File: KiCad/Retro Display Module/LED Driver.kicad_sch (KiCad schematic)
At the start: 30 parts, among them J23 Conn_01x02_Pin, J32 Conn_02x11_Odd_Even, U10 D882_C9634, U11 OP07CDR, U12 D882_C9634, U13 D882_C9634, U14 D882_C9634, U15 D882_C9634, U16 D882_C9634, U17 D882_C9634, U18 D882_C9634, U7 D882_C9634, U8 D882_C9634, U9 D882_C9634

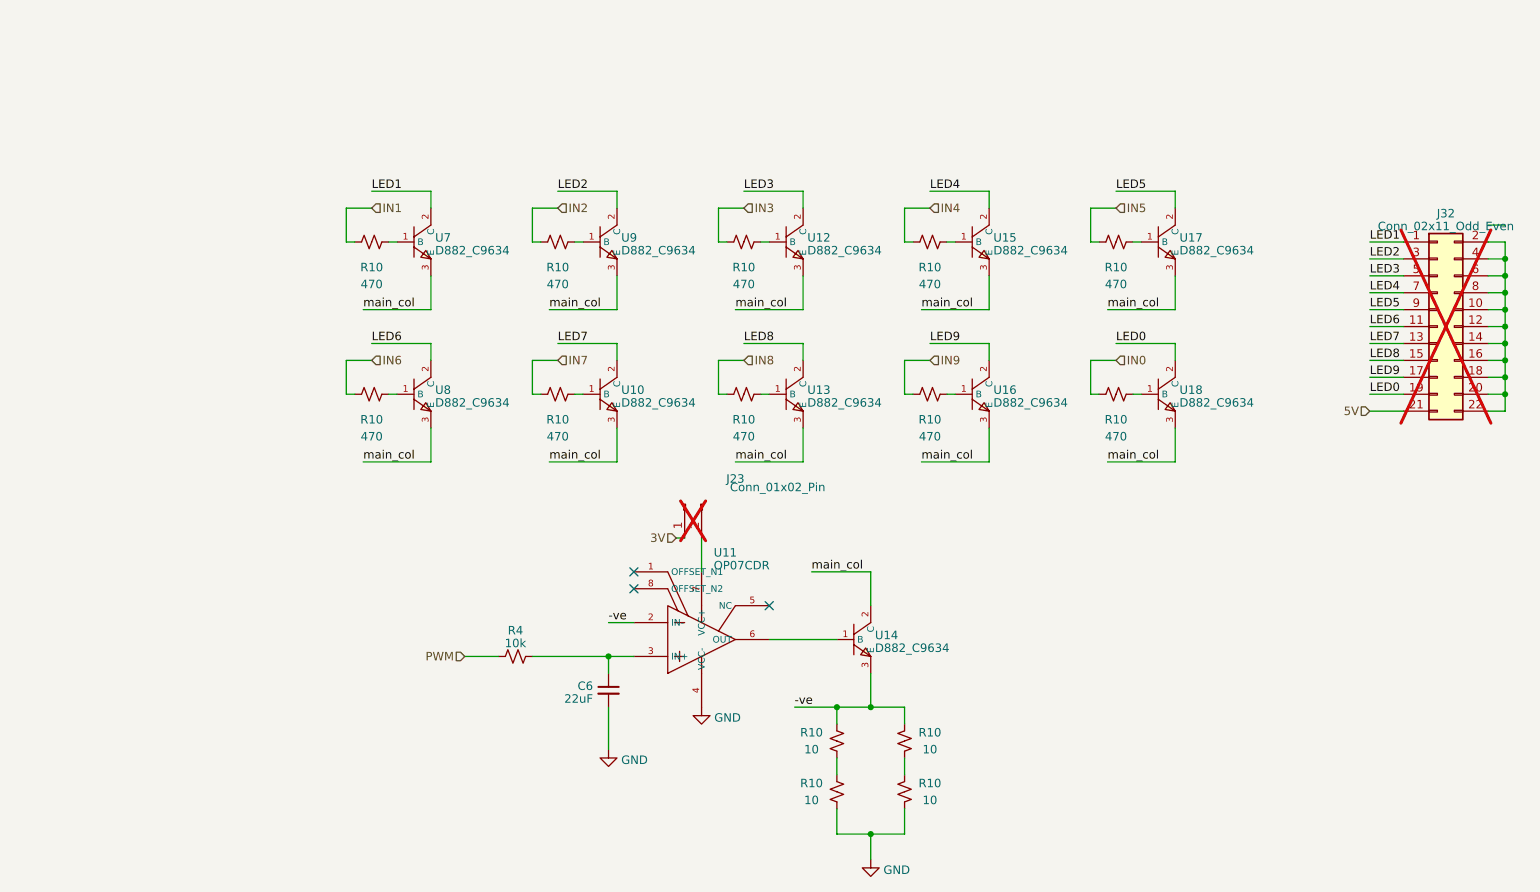
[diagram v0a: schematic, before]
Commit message: Updated USB PD and Driver LED circuit
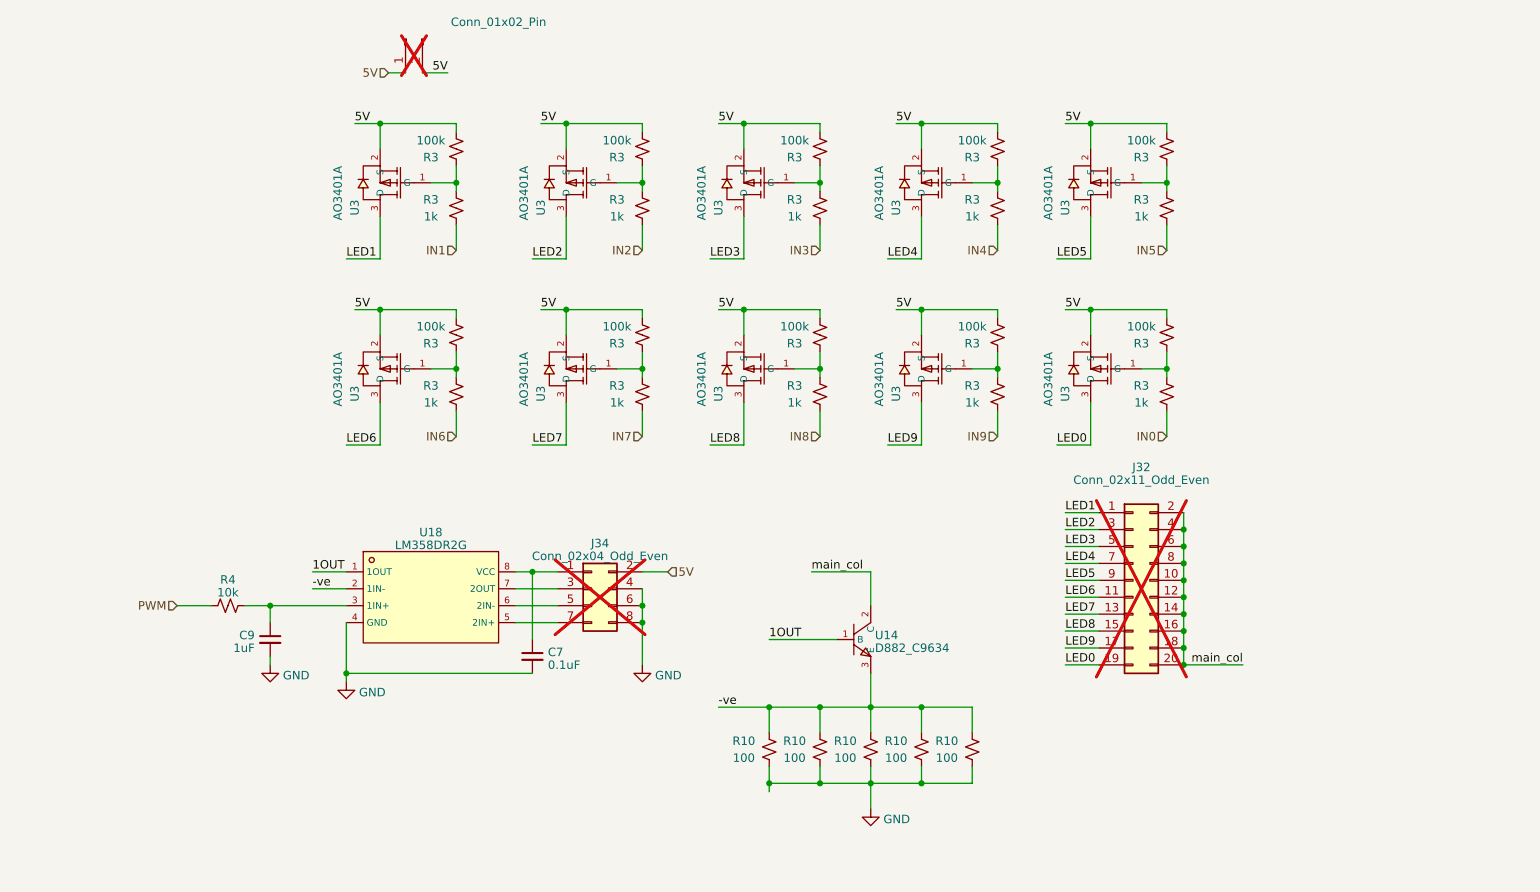
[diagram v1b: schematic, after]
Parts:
- removed C6: 22uF, Capacitor_SMD:C_0805_2012Metric, symbol Device:C_Small
- removed R10 (x10): 470, Resistor_SMD:R_0805_2012Metric, symbol Device:R_Small_US
- removed R10 (x3): 10, Resistor_SMD:R_1206_3216Metric, symbol Device:R_Small_US
- removed U10, U12, U13, U15, U16, U17, U18, U7, U8, U9: D882_C9634, Library:D882, symbol EEE4022S:D882_C9634
- removed U11: OP07CDR, Library:SOIC-8_L4.9-W3.9-P1.27-LS6.0-BL, symbol EEE4022S:OP07CDR
- added C7: 0.1uF, Capacitor_SMD:C_0402_1005Metric, symbol Device:C_Small
- added C9: 1uF, Capacitor_SMD:C_0603_1608Metric, symbol Device:C_Small
- added J34: Conn_02x04_Odd_Even, Connector_PinHeader_2.54mm:PinHeader_2x04_P2.54mm_Vertical, symbol Connector_Generic:Conn_02x04_Odd_Even
- added R10 (x4): 100, Resistor_SMD:R_1206_3216Metric, symbol Device:R_Small_US
- added R3 (x10): 1k, Resistor_SMD:R_0402_1005Metric, symbol Device:R_Small_US
- added R3 (x10): 100k, Resistor_SMD:R_0402_1005Metric, symbol Device:R_Small_US
- added U18: LM358DR2G, Library:Dual LM358, symbol EEE4022S:LM358DR2G
- added U3 (x10): AO3401A, Library:SOT-23_L2.9-W1.3-P1.90-LS2.4-BR, symbol EEE4022S:AO3401A
- J32: footprint Connector_PinHeader_2.54mm:PinHeader_2x11_P2.54mm_Vertical -> Connector_PinHeader_2.54mm:PinHeader_2x10_P2.54mm_Vertical; symbol Connector_Generic:Conn_02x11_Odd_Even -> Connector_Generic:Conn_02x10_Odd_Even; now in the parts list
- R10: value 10 -> 100; LCSC C17903 -> C17901
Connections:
- net 3V is gone; now on net 5V: J23.1 (Pin_1)
- net -ve: now also R10.1, R10.1, R10.1, R10.1, U18.2 (1IN-)
- net 5V: now also J23.2 (Pin_2), J34.2 (Pin_2), R3.1, R3.1, R3.1, R3.1, R3.1, R3.1, R3.1, R3.1, R3.1, R3.1, U3.2 (S), U3.2 (S), U3.2 (S), U3.2 (S), U3.2 (S), U3.2 (S), U3.2 (S), U3.2 (S), U3.2 (S), U3.2 (S); no longer J32.21 (Pin_21)
- net GND: now also R10.2, C7.2, C9.2, J34.4 (Pin_4), J34.6 (Pin_6), J34.8 (Pin_8), R10.2, R10.2, R10.2, R10.2, U18.4 (GND)
- net IN0: now also R3.2
- net IN1: now also R3.2
- net IN2: now also R3.2
- net IN3: now also R3.2
- net IN4: now also R3.2
- net IN5: now also R3.2
- net IN6: now also R3.2
- net IN7: now also R3.2
- net IN8: now also R3.2
- net IN9: now also R3.2
- net LED0: now also U3.3 (D)
- net LED1: now also U3.3 (D)
- net LED2: now also U3.3 (D)
- net LED3: now also U3.3 (D)
- net LED4: now also U3.3 (D)
- net LED5: now also U3.3 (D)
- net LED6: now also U3.3 (D)
- net LED7: now also U3.3 (D)
- net LED8: now also U3.3 (D)
- net LED9: now also U3.3 (D)
- net main_col: now also J32.10 (Pin_10), J32.12 (Pin_12), J32.14 (Pin_14), J32.16 (Pin_16), J32.18 (Pin_18), J32.2 (Pin_2), J32.20 (Pin_20), J32.4 (Pin_4), J32.6 (Pin_6), J32.8 (Pin_8)
- net at R4.1: now also C9.1, U18.3 (1IN+)
- net 1OUT: now reaches U14.1 (B)
- net 1OUT: now also U18.1 (1OUT)
- new net: R3.1, R3.2, U3.1 (G) (x10)
- new net: C7.1, J34.1 (Pin_1), U18.8 (VCC)
- new net: J34.3 (Pin_3), U18.7 (2OUT)
- new net: J34.5 (Pin_5), U18.6 (2IN-)
- new net: J34.7 (Pin_7), U18.5 (2IN+)
- no-connect marks 3 -> 0
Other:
- moved on the sheet: R10, R4

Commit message: Updated Display Board schematic and Ltspice simulations
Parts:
- removed U3 (x10): AO3401A, Library:SOT-23_L2.9-W1.3-P1.90-LS2.4-BR, symbol EEE4022S:AO3401A
- added J25: Conn_02x03_Odd_Even, Connector_PinHeader_2.54mm:PinHeader_2x03_P2.54mm_Vertical, symbol Connector_Generic:Conn_02x03_Odd_Even
- added TP5: TestPoint, Library:TestPoint_THTPad_2.0x2.0mm_Drill1.0mm, symbol Connector:TestPoint
- added U3 (x10): AO3401A, Library:SOT-23_L2.9-W1.3-P1.90-LS2.4-BR, symbol EEE4022S:AO3401A
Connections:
- net -ve: now also J25.3 (Pin_3), TP5.1; no longer U18.2 (1IN-)
- net 1OUT: now also J25.1 (Pin_1); no longer U18.1 (1OUT)
- net 5V: now also U3.2 (S), U3.2 (S), U3.2 (S), U3.2 (S), U3.2 (S), U3.2 (S), U3.2 (S), U3.2 (S), U3.2 (S), U3.2 (S)
- net LED0: now also U3.3 (D)
- net LED1: now also U3.3 (D)
- net LED2: now also U3.3 (D)
- net LED3: now also U3.3 (D)
- net LED4: now also U3.3 (D)
- net LED5: now also U3.3 (D)
- net LED6: now also U3.3 (D)
- net LED7: now also U3.3 (D)
- net LED8: now also U3.3 (D)
- net LED9: now also U3.3 (D)
- net at R3.1, R3.2: now also U3.1 (G) (x10)
- net at C9.1, R4.1: now also J25.5 (Pin_5); no longer U18.3 (1IN+)
- new net: J25.2 (Pin_2), U18.1 (1OUT)
- new net: J25.4 (Pin_4), U18.2 (1IN-)
- new net: J25.6 (Pin_6), U18.3 (1IN+)
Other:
- moved on the sheet: C9, R4

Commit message: Updated Display PCB
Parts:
- removed U14: D882_C9634, Library:D882, symbol EEE4022S:D882_C9634
- added U17: MJD44H11J, Library:MJD44 NPN, symbol EEE4022S:MJD44H11J
- renumbered J34 to J33, J32 to J34, U18 to U12
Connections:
- net -ve: now also U17.3 (E)
- net 1OUT: now also J25.5 (Pin_5), U17.1 (B); no longer J25.1 (Pin_1)
- net main_col: now also U17.2 (C)
- net at C9.1, R4.1: now also J25.1 (Pin_1); no longer J25.5 (Pin_5)
- net at J25.2 (Pin_2): now also U12.3 (1IN+); no longer U12.1 (1OUT)
- net at J25.6 (Pin_6): now also U12.1 (1OUT); no longer U12.3 (1IN+)
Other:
- moved on the sheet: C9, J25, R4

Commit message: Updated Display PCB
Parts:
- C7: footprint Capacitor_SMD:C_0402_1005Metric -> Library:C_0402_1005Metric
- R3: footprint Resistor_SMD:R_0402_1005Metric -> Library:R_0402_1005Metric
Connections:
- net 5V: no longer J23.2 (Pin_2), R3.1, R3.1, R3.1, R3.1, R3.1, R3.1, R3.1, R3.1, R3.1, R3.1, U3.2 (S), U3.2 (S), U3.2 (S), U3.2 (S), U3.2 (S), U3.2 (S), U3.2 (S), U3.2 (S), U3.2 (S), U3.2 (S)
- net LED0: now also J34.1 (Pin_1); no longer J34.19 (Pin_19)
- net LED1: now also J34.19 (Pin_19); no longer J34.1 (Pin_1)
- net LED2: now also J34.17 (Pin_17); no longer J34.3 (Pin_3)
- net LED3: now also J34.15 (Pin_15); no longer J34.5 (Pin_5)
- net LED4: now also J34.13 (Pin_13); no longer J34.7 (Pin_7)
- net LED5: now also J34.11 (Pin_11); no longer J34.9 (Pin_9)
- net LED6: now also J34.9 (Pin_9); no longer J34.11 (Pin_11)
- net LED7: now also J34.7 (Pin_7); no longer J34.13 (Pin_13)
- net LED8: now also J34.5 (Pin_5); no longer J34.15 (Pin_15)
- net LED9: now also J34.3 (Pin_3); no longer J34.17 (Pin_17)
- new net 5V_PWR: J23.2 (Pin_2), R3.1, R3.1, R3.1, R3.1, R3.1, R3.1, R3.1, R3.1, R3.1, R3.1, U3.2 (S), U3.2 (S), U3.2 (S), U3.2 (S), U3.2 (S), U3.2 (S), U3.2 (S), U3.2 (S), U3.2 (S), U3.2 (S)

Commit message: Begin STM32 Programming
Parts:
- added JP1: Jumper_2_Open, Jumper:SolderJumper-2_P1.3mm_Open_RoundedPad1.0x1.5mm, symbol Jumper:Jumper_2_Open
- added R10 (x5): 100, Resistor_SMD:R_1206_3216Metric, symbol Device:R_Small_US
- J23, J34: now left out of the parts list
- R3: footprint Library:R_0402_1005Metric -> Library:R_0402_1005Metric_Pad0.72x0.64mm_HandSolder
- TP5: now not fitted; now left out of the parts list
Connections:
- net -ve: now also JP1.1 (A)
- net GND: now also R10.2, R10.2, R10.2, R10.2, R10.2
- new net: JP1.2 (B), R10.1, R10.1, R10.1, R10.1, R10.1
